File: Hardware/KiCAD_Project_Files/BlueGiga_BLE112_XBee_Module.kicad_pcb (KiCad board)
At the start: 2 copper layers, 24.5 x 24.4 mm, 16 parts, among them J2 HEADER_F_XBEE_PTH, P1 HEADER_1X8, P2 HEADER_1X3, P3 HEADER_1X8, P4 HEADER_1X2, P5 HEADER_1X10, U1 BLE112-A, U2 AAT3221

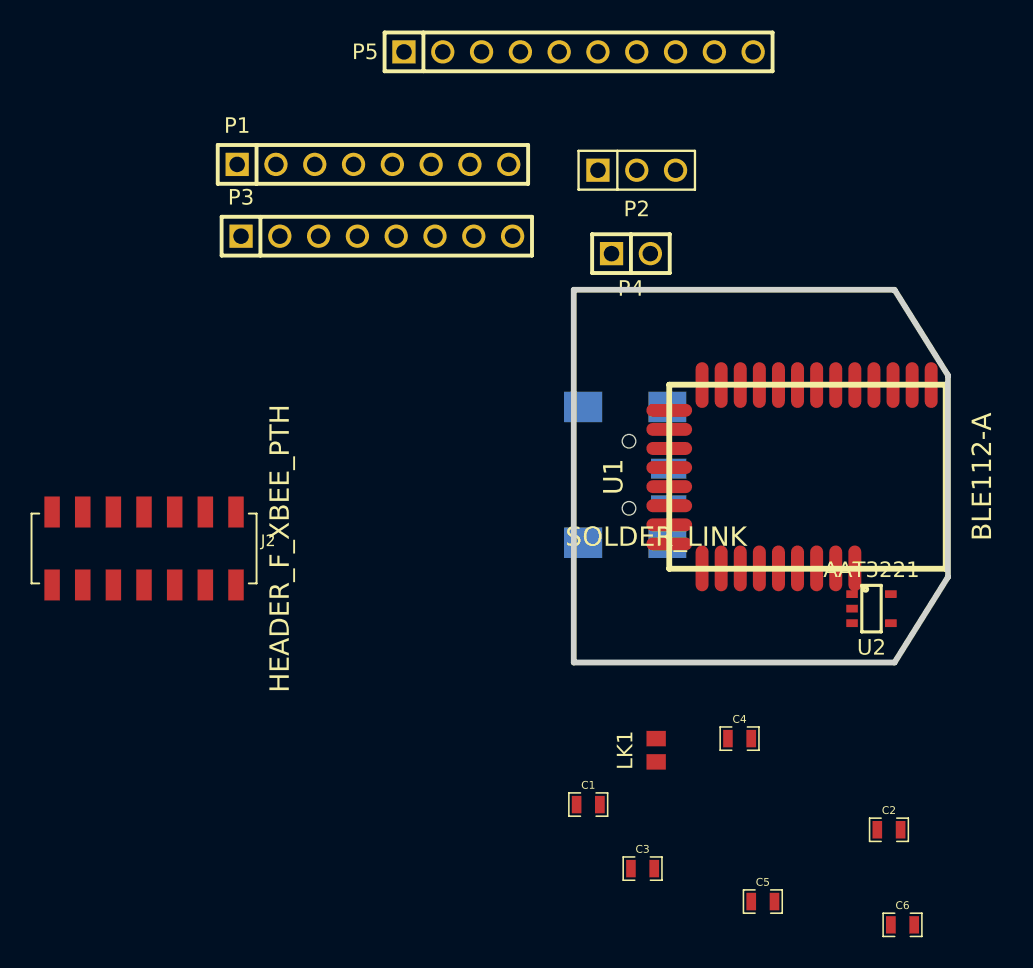
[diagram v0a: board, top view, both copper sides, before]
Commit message: Updated Schematic to add debug header and remove unused pin headers.  PCB needs a few routes still and clean up debug header area.
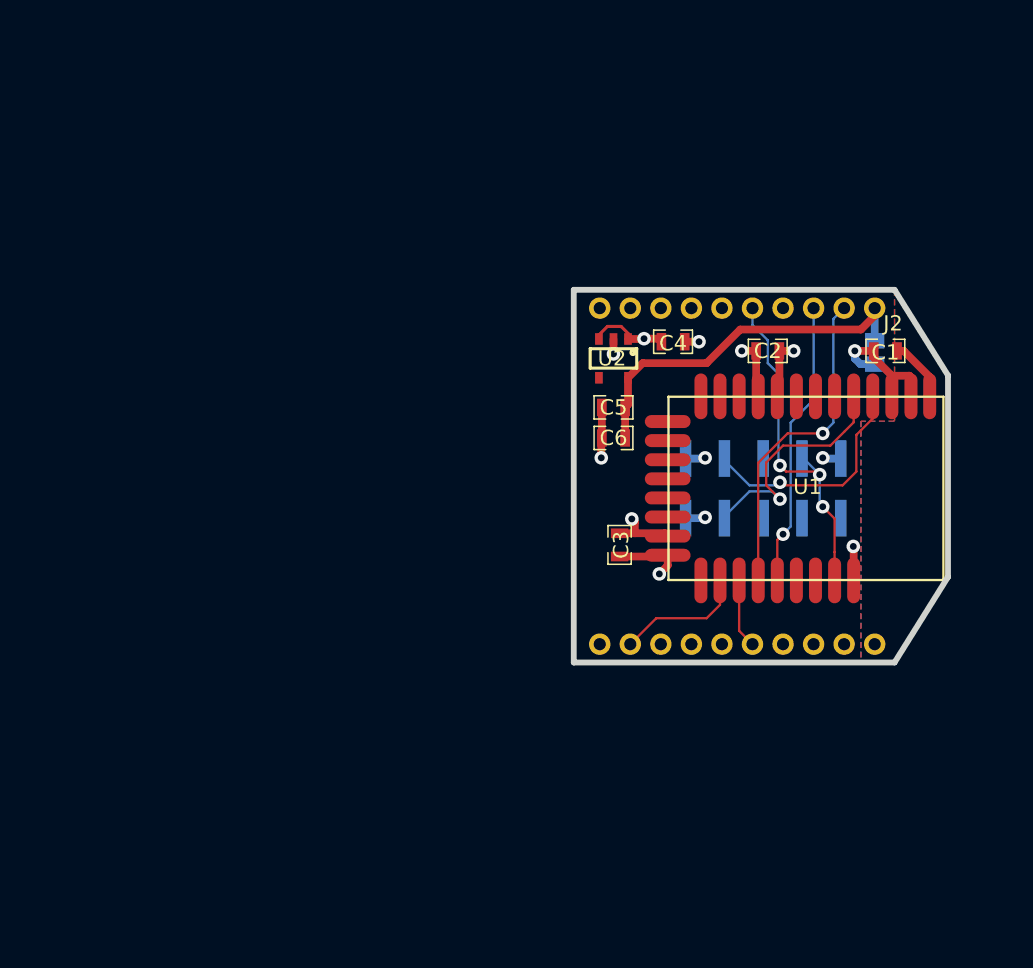
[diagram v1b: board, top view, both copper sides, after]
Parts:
- removed J1: , CONNECTOR_USB_TYPE_MINI_B_RA_F_SMT_MOLEX
- removed P2: HEADER_1X3, HEADER_100MIL_1R3P_PTH
- removed P3: HEADER_1X8, HEADER_100MIL_1R8P_PTH
- removed P4: HEADER_1X2, HEADER_100MIL_1R2P_PTH
- removed P5: HEADER_1X10, HEADER_100MIL_1R10P_PTH
- J2: footprint HEADER_F_2x7_2MM -> HEADER_XBEE
- LK1: moved to B.Cu
- P1: value HEADER_1X8 -> HEADER_2X5; footprint HEADER_100MIL_1R8P_PTH -> HEADER_50MIL_2R10P_SMT; moved to B.Cu
- moved J2 48.1 mm to (118.7, 92.8), turned to 270 degrees
- moved C6 37.1 mm to (101.6, 90.3), turned to 180 degrees
- moved C1 35.5 mm to (119.4, 84.6)
- moved C5 33.8 mm to (101.6, 88.3), turned to 180 degrees
- moved P1 33.2 mm to (111.4, 93.6)
- moved C2 32.3 mm to (111.7, 84.6), turned to 180 degrees
- moved LK1 29.7 mm to (118.7, 84.7)
- moved C4 26.3 mm to (105.5, 84.0)
- moved U2 23.5 mm to (101.6, 85.1), turned to 270 degrees
- moved C3 21.2 mm to (102.0, 97.3), turned to 270 degrees
- moved U1 0.77 mm to (114.2, 93.6)
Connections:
- C5 pad 1: N-0000040 -> VCC
- C6 pad 1: N-0000040 -> VCC
- J2 pad 1: N-0000040 -> VCC
- J2 pad 11: N-0000026 -> (no net)
- J2 pad 13: N-0000022 -> (no net)
- J2 pad 4: N-0000025 -> (no net)
- J2 pad 6: N-0000018 -> (no net)
- J2 pad 7: N-0000024 -> (no net)
- J2 pad 8: N-0000020 -> (no net)
- J2 pad 9: N-0000023 -> (no net)
- LK1 pad 2: N-0000040 -> VCC
- P1 pad 1: N-000004 -> GND
- P1 pad 2: N-000005 -> +3.3V
- P1 pad 3: RX -> P2_2
- P1 pad 4: TX -> P2_1
- P1 pad 5: CT -> (no net)
- P1 pad 6: RT -> (no net)
- P1 pad 7: N-0000017 -> RESET
- P1 pad 8: N-0000015 -> (no net)
- U1 pad 11: N-000007 -> (no net)
- U1 pad 12: N-0000032 -> (no net)
- U1 pad 13: N-0000010 -> (no net)
- U1 pad 14: N-0000011 -> (no net)
- U1 pad 15: N-0000012 -> (no net)
- U1 pad 16: N-0000013 -> (no net)
- U1 pad 17: N-0000014 -> (no net)
- U1 pad 18: N-000006 -> (no net)
- U1 pad 19: N-0000015 -> (no net)
- U1 pad 22: N-0000017 -> (no net)
- U1 pad 27: N-000005 -> (no net)
- U1 pad 28: N-000004 -> (no net)
- U1 pad 4: N-000003 -> P2_2
- U1 pad 5: N-000002 -> P2_1
- U1 pad 6: N-000001 -> (no net)
- U1 pad 7: N-000008 -> (no net)
- U1 pad 8: N-000009 -> (no net)
- U2 pad 1: N-0000040 -> +3.3V
- U2 pad 3: N-0000040 -> +3.3V
- U2 pad 5: +3.3V -> VCC
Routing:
- net +3.3V: track 0.00 -> 26.5 mm, vias 0 -> 6
- net VCC: track 0.00 -> 24.5 mm
- net RESET: track 0.00 -> 22.8 mm, vias 0 -> 3
- net TX: track 0.00 -> 21.5 mm, vias 0 -> 1
- net GND: track 0.00 -> 21.5 mm, vias 0 -> 7
- net RX: track 0.00 -> 18.8 mm, vias 0 -> 1
- net P2_1: track 0.00 -> 16.0 mm, vias 0 -> 1
- net P2_2: track 0.00 -> 15.3 mm, vias 0 -> 1
- net RT: track 0.00 -> 8.54 mm
- net CT: track 0.00 -> 4.54 mm
- added copper zone on B.Cu, net (none)
- added copper zone on F.Cu, net (none)
- added copper zone on Inner2-Pwr.Cu, net +3.3V
- added copper zone on Inner3-Gnd.Cu, net GND
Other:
- copper layers 2 -> 4
- net class Default: clearance 0.254 -> 0.1524; trace_width 0.2032 -> 0.1524
- net class Power added: clearance 0.1524, trace_width 0.508, via_dia 0.889, via_drill 0.635
- rule trace_clearance: 0.254 -> 0.1524
- rule trace_min: 0.2032 -> 0.1524

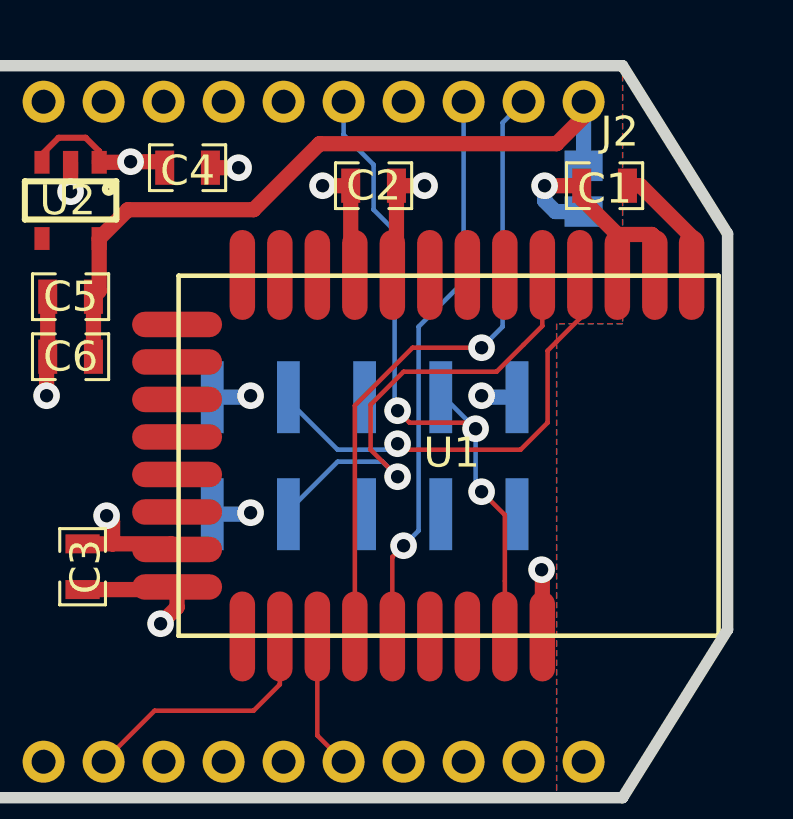
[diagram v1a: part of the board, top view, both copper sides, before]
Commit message: Rotated debug header 180 deg for better routing. Added dimensions to PCB. Board is 100% routed with good DRC. Need to generate gerbers and visually check each layer.
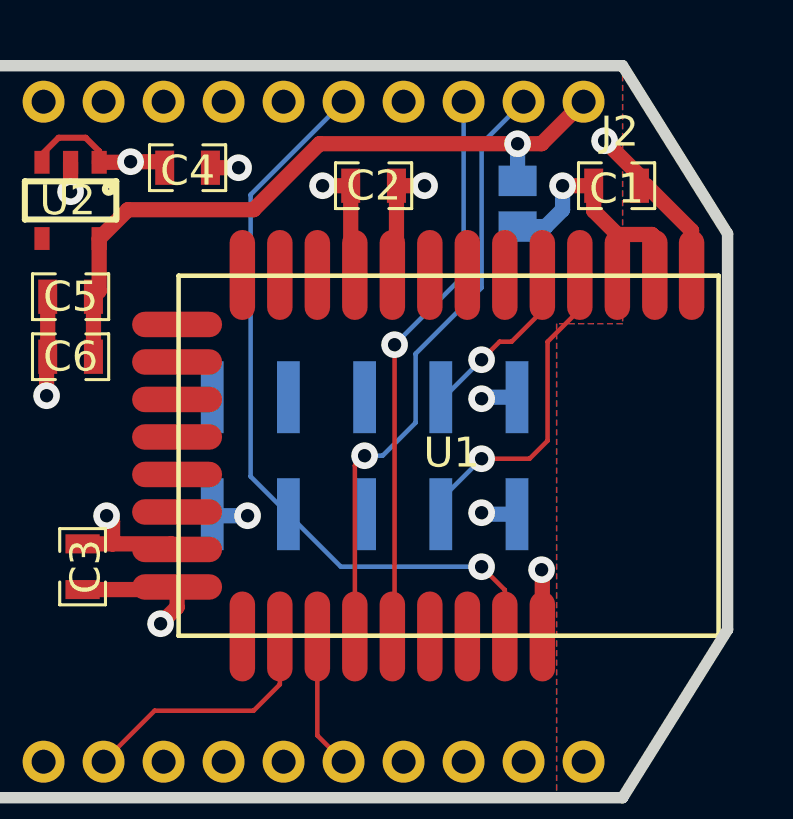
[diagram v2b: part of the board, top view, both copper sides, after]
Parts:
- moved LK1 2.26 mm to (116.5, 85.2)
- moved C1 0.40 mm to (119.8, 84.6)
- turned P1 to 180 degrees
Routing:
- net P2_1: track 16.0 -> 5.78 mm
- net P2_2: track 15.3 -> 10.8 mm
- net RESET: track 22.8 -> 25.5 mm, vias 3 -> 1
- net GND: track 21.5 -> 23.1 mm, vias 7 -> 8
- net +3.3V: track 26.5 -> 28.0 mm
- net VCC: track 24.5 -> 23.3 mm, vias 0 -> 1
- net TX: track 21.5 -> 20.5 mm
